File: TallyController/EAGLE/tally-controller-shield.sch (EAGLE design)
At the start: 27 parts, among them J2 Mega R3, U1 SN75174N, U2 SN75174N, U3 SN75174N

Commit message: Add external power input to power all the external bits.  Fix DRC errors that I didn't catch for some reason.
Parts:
- added EXTPOWER: 22-23-2021, con-molex:22-23-2021
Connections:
- new net VCC: EXTPOWER-2.S, JP1.3, JP4.2, NEOPIXEL-2.S, R1.2, U1.VCC, U2.VCC, U3.VCC
- net 5V@0: no longer JP1.3, JP4.2, NEOPIXEL-2.S, R1.2, U1.VCC
- net 5V@1: no longer U2.VCC, U3.VCC
- net GND: now also EXTPOWER-1.S
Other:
- note added: "1.2"
- note removed: "1.1"

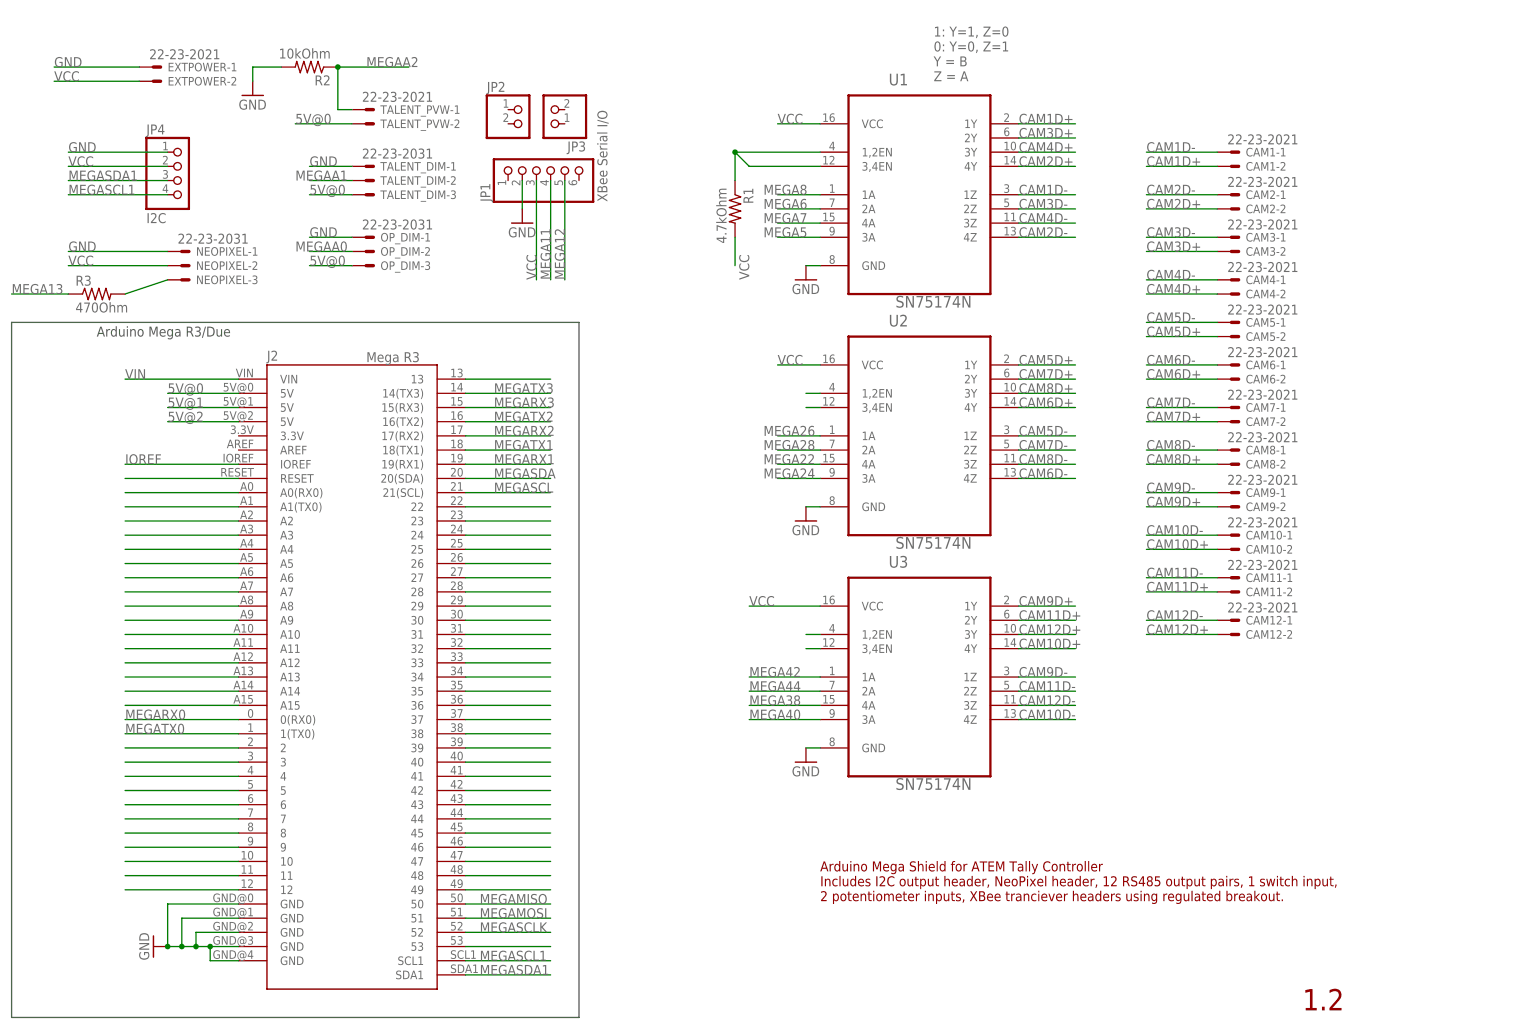
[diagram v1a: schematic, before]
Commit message: Fix the non SMD version of the controller as well.
Also add pads for terminators at the controller.
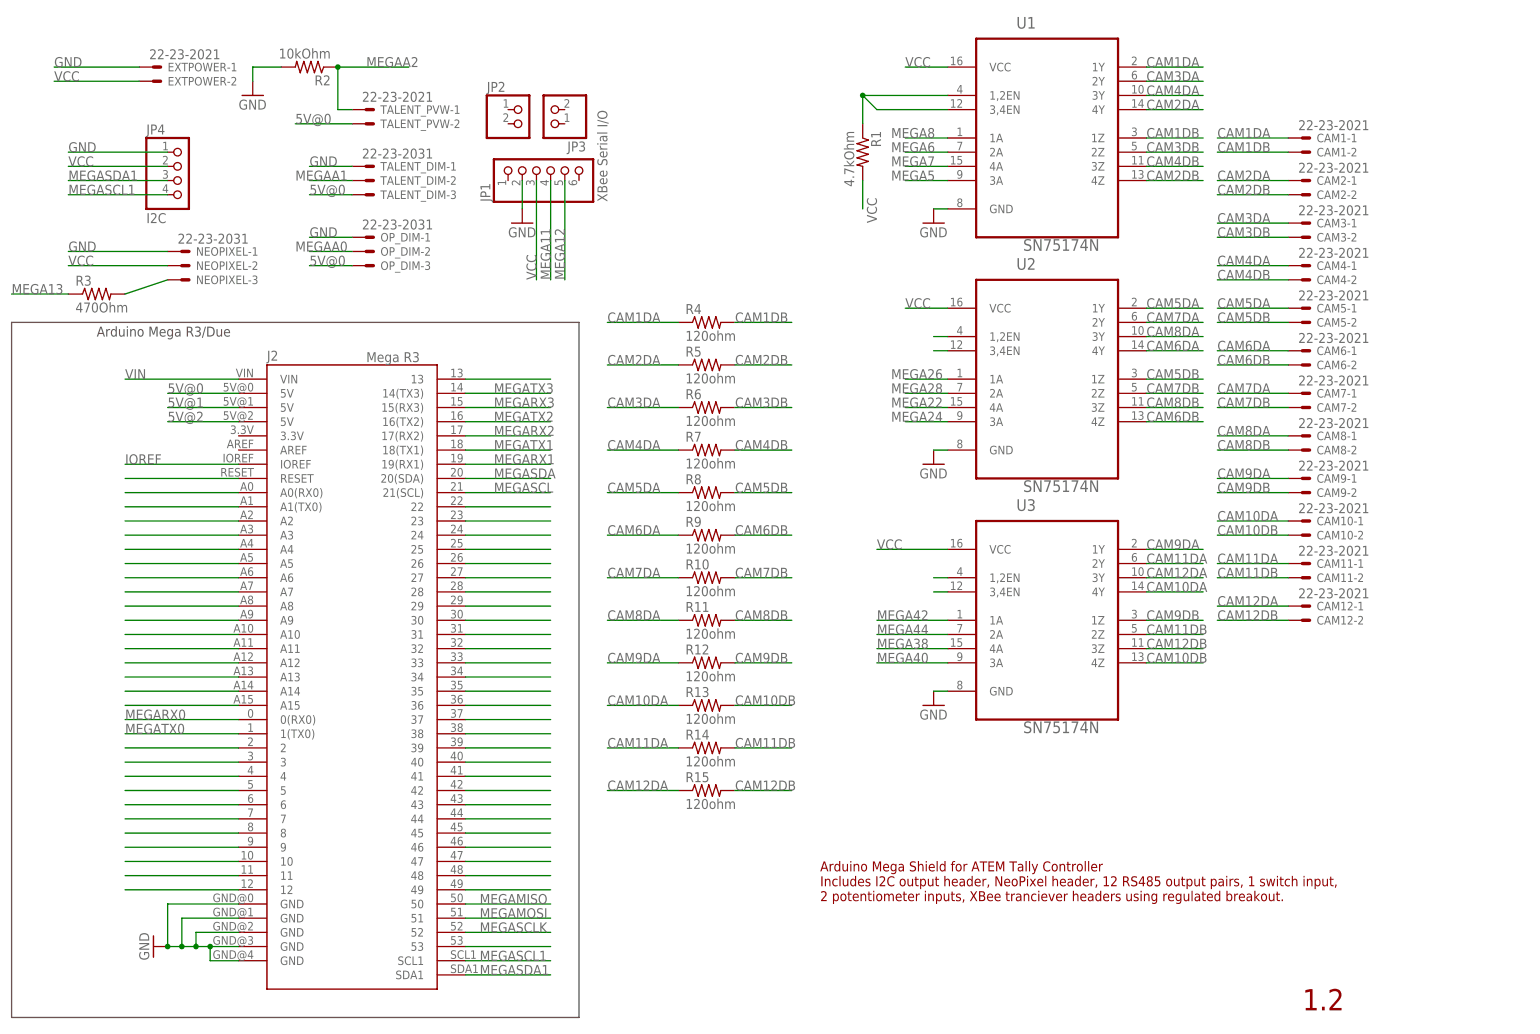
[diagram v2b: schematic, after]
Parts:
- added R10, R11, R12, R13, R14, R15, R4, R5, R6, R7, R8, R9: 120ohm, rcl:R-US_R0805
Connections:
- removed net CAM10D+: CAM10-2.S, U3.4Y
- removed net CAM10D-: CAM10-1.S, U3.4Z
- removed net CAM11D+: CAM11-2.S, U3.2Y
- removed net CAM11D-: CAM11-1.S, U3.2Z
- removed net CAM12D+: CAM12-2.S, U3.3Y
- removed net CAM12D-: CAM12-1.S, U3.3Z
- removed net CAM1D+: CAM1-2.S, U1.1Y
- removed net CAM1D-: CAM1-1.S, U1.1Z
- removed net CAM2D+: CAM2-2.S, U1.4Y
- removed net CAM2D-: CAM2-1.S, U1.4Z
- removed net CAM3D+: CAM3-2.S, U1.2Y
- removed net CAM3D-: CAM3-1.S, U1.2Z
- removed net CAM4D+: CAM4-2.S, U1.3Y
- removed net CAM4D-: CAM4-1.S, U1.3Z
- removed net CAM5D+: CAM5-2.S, U2.1Y
- removed net CAM5D-: CAM5-1.S, U2.1Z
- removed net CAM6D+: CAM6-2.S, U2.4Y
- removed net CAM6D-: CAM6-1.S, U2.4Z
- removed net CAM7D+: CAM7-2.S, U2.2Y
- removed net CAM7D-: CAM7-1.S, U2.2Z
- removed net CAM8D+: CAM8-2.S, U2.3Y
- removed net CAM8D-: CAM8-1.S, U2.3Z
- removed net CAM9D+: CAM9-2.S, U3.1Y
- removed net CAM9D-: CAM9-1.S, U3.1Z
- new net CAM10DA: CAM10-1.S, R13.1, U3.4Y
- new net CAM10DB: CAM10-2.S, R13.2, U3.4Z
- new net CAM11DA: CAM11-1.S, R14.1, U3.2Y
- new net CAM11DB: CAM11-2.S, R14.2, U3.2Z
- new net CAM12DA: CAM12-1.S, R15.1, U3.3Y
- new net CAM12DB: CAM12-2.S, R15.2, U3.3Z
- new net CAM1DA: CAM1-1.S, R4.1, U1.1Y
- new net CAM1DB: CAM1-2.S, R4.2, U1.1Z
- new net CAM2DA: CAM2-1.S, R5.1, U1.4Y
- new net CAM2DB: CAM2-2.S, R5.2, U1.4Z
- new net CAM3DA: CAM3-1.S, R6.1, U1.2Y
- new net CAM3DB: CAM3-2.S, R6.2, U1.2Z
- new net CAM4DA: CAM4-1.S, R7.1, U1.3Y
- new net CAM4DB: CAM4-2.S, R7.2, U1.3Z
- new net CAM5DA: CAM5-1.S, R8.1, U2.1Y
- new net CAM5DB: CAM5-2.S, R8.2, U2.1Z
- new net CAM6DA: CAM6-1.S, R9.1, U2.4Y
- new net CAM6DB: CAM6-2.S, R9.2, U2.4Z
- new net CAM7DA: CAM7-1.S, R10.1, U2.2Y
- new net CAM7DB: CAM7-2.S, R10.2, U2.2Z
- new net CAM8DA: CAM8-1.S, R11.1, U2.3Y
- new net CAM8DB: CAM8-2.S, R11.2, U2.3Z
- new net CAM9DA: CAM9-1.S, R12.1, U3.1Y
- new net CAM9DB: CAM9-2.S, R12.2, U3.1Z
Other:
- note removed: "1: Y=1, Z=0 0: Y=0, Z=1 Y = B Z = A"
- moved on the sheet: CAM1-1, CAM1-2, CAM10-1, CAM10-2, CAM11-1, CAM11-2, CAM12-1, CAM12-2, CAM2-1, CAM2-2, CAM3-1, CAM3-2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
